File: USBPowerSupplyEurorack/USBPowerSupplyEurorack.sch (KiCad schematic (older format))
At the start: 19 parts, among them J1 1734366-1, J2 10129381-910001BLF, Q1 Q_PMOS_GSD

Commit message: connected switch to control the DC-DC converters
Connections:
- net labels added: CTRL
- net labels removed: +5VD
- no-connect marks 8 -> 6
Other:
- moved on the sheet: R1, S1
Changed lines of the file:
@@
 USB Power In
 Wire Wire Line
-	4430 1830 4430 1930
-Wire Wire Line
-	5830 1830 5830 1930
+	4690 1830 4690 1930
+Wire Wire Line
+	6090 1830 6090 1930
 $Comp
 L LP4OA1PBCTR:LP4OA1PBCTR S1
 U 1 1 5FE10AE7
-P 5130 2530
-F 0 "S1" V 6270 2840 50  0000 L CNN
-F 1 "LP4OA1PBCTR" V 6180 2640 50  0000 L CNN
-F 2 "LP4OA1PBCTR:LP4OA1PBCTR" H 6180 3030 50  0001 L CNN
-F 3 "http://spec_sheets.e-switch.com/specs/B240001.pdf" H 6180 2930 50  0001 L CNN
-F 4 "Pushbutton Switches DPDT On-Mom LED, Red" H 6180 2830 50  0001 L CNN "Description"
-F 5 "19.95" H 6180 2730 50  0001 L CNN "Height"
-F 6 "E-Switch" H 6180 2630 50  0001 L CNN "Manufacturer_Name"
-F 7 "LP4OA1PBCTR" H 6180 2530 50  0001 L CNN "Manufacturer_Part_Number"
-F 8 "" H 6180 2430 50  0001 L CNN "Arrow Part Number"
-F 9 "" H 6180 2330 50  0001 L CNN "Arrow Price/Stock"
-F 10 "612-LP4OA1PBCTR" H 6180 2230 50  0001 L CNN "Mouser Part Number"
-F 11 "https://www.mouser.com/Search/Refine.aspx?Keyword=612-LP4OA1PBCTR" H 6180 2130 50  0001 L CNN "Mouser Price/Stock"
-	1    5130 2530
+P 5390 2530
+F 0 "S1" V 6530 2840 50  0000 L CNN
+F 1 "LP4OA1PBCTR" V 6440 2640 50  0000 L CNN
+F 2 "LP4OA1PBCTR:LP4OA1PBCTR" H 6440 3030 50  0001 L CNN
+F 3 "http://spec_sheets.e-switch.com/specs/B240001.pdf" H 6440 2930 50  0001 L CNN
+F 4 "Pushbutton Switches DPDT On-Mom LED, Red" H 6440 2830 50  0001 L CNN "Description"
+F 5 "19.95" H 6440 2730 50  0001 L CNN "Height"
+F 6 "E-Switch" H 6440 2630 50  0001 L CNN "Manufacturer_Name"
+F 7 "LP4OA1PBCTR" H 6440 2530 50  0001 L CNN "Manufacturer_Part_Number"
+F 8 "" H 6440 2430 50  0001 L CNN "Arrow Part Number"
+F 9 "" H 6440 2330 50  0001 L CNN "Arrow Price/Stock"
+F 10 "612-LP4OA1PBCTR" H 6440 2230 50  0001 L CNN "Mouser Part Number"
+F 11 "https://www.mouser.com/Search/Refine.aspx?Keyword=612-LP4OA1PBCTR" H 6440 2130 50  0001 L CNN "Mouser Price/Stock"
+	1    5390 2530
 	0    -1   -1   0
 $EndComp
-NoConn ~ 4430 2030
-NoConn ~ 5830 2030
-Connection ~ 5830 1830
-$Comp
-L power:+5VD #PWR0102
-U 1 1 5FE20BD7
-P 2560 1440
-F 0 "#PWR0102" H 2560 1290 50  0001 C CNN
-F 1 "+5VD" H 2575 1613 50  0000 C CNN
-F 2 "" H 2560 1440 50  0001 C CNN
-F 3 "" H 2560 1440 50  0001 C CNN
-	1    2560 1440
-	1    0    0    -1
-$EndComp
+NoConn ~ 4690 2030
+NoConn ~ 6090 2030
+Connection ~ 6090 1830
 $Comp
 L power:+5V #PWR0103
 U 1 1 5FE2195B
-P 5830 1830
-F 0 "#PWR0103" H 5830 1680 50  0001 C CNN
-F 1 "+5V" H 5845 2003 50  0000 C CNN
-F 2 "" H 5830 1830 50  0001 C CNN
-F 3 "" H 5830 1830 50  0001 C CNN
-	1    5830 1830
-	1    0    0    -1
-$EndComp
-$Comp
-L power:+5VD #PWR0104
-U 1 1 5FE220CC
-P 4430 1830
-F 0 "#PWR0104" H 4430 1680 50  0001 C CNN
-F 1 "+5VD" H 4445 2003 50  0000 C CNN
-F 2 "" H 4430 1830 50  0001 C CNN
-F 3 "" H 4430 1830 50  0001 C CNN
-	1    4430 1830
-	1    0    0    -1
-$EndComp
-Connection ~ 4430 1830
+P 6090 1830
+F 0 "#PWR0103" H 6090 1680 50  0001 C CNN
+F 1 "+5V" H 6105 2003 50  0000 C CNN
+F 2 "" H 6090 1830 50  0001 C CNN
+F 3 "" H 6090 1830 50  0001 C CNN
+	1    6090 1830
+	1    0    0    -1
+$EndComp
 $Comp
 L Device:R_Small R1
 U 1 1 5FE234A2
-P 5130 2630
-F 0 "R1" H 5189 2676 50  0000 L CNN
-F 1 "510" H 5189 2585 50  0000 L CNN
-F 2 "Resistor_SMD:R_0612_1632Metric" H 5130 2630 50  0001 C CNN
-F 3 "~" H 5130 2630 50  0001 C CNN
-	1    5130 2630
-	1    0    0    -1
-$EndComp
-Wire Notes Line
-	4240 1010 6360 1010
+P 5390 2630
+F 0 "R1" H 5449 2676 50  0000 L CNN
+F 1 "510" H 5449 2585 50  0000 L CNN
+F 2 "Resistor_SMD:R_0612_1632Metric" H 5390 2630 50  0001 C CNN
+F 3 "~" H 5390 2630 50  0001 C CNN
+	1    5390 2630
+	1    0    0    -1
+$EndComp
 Wire Notes Line
 	6360 1010 6360 3050
-Wire Notes Line
-	6360 3050 4240 3050
-Wire Notes Line
-	4240 3050 4240 1010
 Text Notes 4240 1010 0    50   ~ 0
 Push button & LED
@@
 $EndComp
 Connection ~ 5990 5650
-$Comp
-L power:PWR_FLAG #FLG0104
-U 1 1 5FEBEC19
-P 5830 1830
-F 0 "#FLG0104" H 5830 1905 50  0001 C CNN
-F 1 "PWR_FLAG" V 5830 1958 50  0000 L CNN
-F 2 "" H 5830 1830 50  0001 C CNN
-F 3 "~" H 5830 1830 50  0001 C CNN
-	1    5830 1830
-	0    1    1    0
-$EndComp
 Wire Wire Line
 	8900 5530 9800 5530
@@
 	0    1    1    0
 $EndComp
-$Comp
-L RS6-0512S:RS6-0512S PS1
-U 1 1 5FE5CD2D
-P 1630 4780
-F 0 "PS1" H 1990 5020 50  0000 L CNN
-F 1 "RS6-0512S" H 1920 4940 50  0000 L CNN
-F 2 "RS6-0512S:RS60512S" H 2480 4880 50  0001 L CNN
-F 3 "https://componentsearchengine.com/Datasheets/1/RS6-0512S.pdf" H 2480 4780 50  0001 L CNN
-F 4 "Isolated DC/DC Converters 6W 4.5-9Vin 12Vout 500mA SIP8" H 2480 4680 50  0001 L CNN "Description"
-F 5 "11.6" H 2480 4580 50  0001 L CNN "Height"
-F 6 "RECOM Power" H 2480 4480 50  0001 L CNN "Manufacturer_Name"
-F 7 "RS6-0512S" H 2480 4380 50  0001 L CNN "Manufacturer_Part_Number"
-F 8 "919-RS6-0512S" H 2480 4280 50  0001 L CNN "Mouser Part Number"
-F 9 "https://www.mouser.co.uk/ProductDetail/RECOM-Power/RS6-0512S?qs=FLBwGrBR9%252B1rp7zTwCRMhw%3D%3D" H 2480 4180 50  0001 L CNN "Mouser Price/Stock"
-F 10 "" H 2480 4080 50  0001 L CNN "Arrow Part Number"
-F 11 "" H 2480 3980 50  0001 L CNN "Arrow Price/Stock"
-	1    1630 4780
-	1    0    0    -1
-$EndComp
 Text GLabel 1630 4780 0    50   Input ~ 0
 -Vin
 Text GLabel 1630 4880 0    50   Input ~ 0
 +Vin
-NoConn ~ 1630 4980
 Text GLabel 1560 5280 0    50   Input ~ 0
 0V
@@
 Text GLabel 1630 5920 0    50   Input ~ 0
 +Vin
-NoConn ~ 1630 6020
 Text GLabel 1560 6220 0    50   Input ~ 0
 0V
@@
 	1    0    0    -1
 $EndComp
-Text GLabel 5080 2880 0    50   Input ~ 0
+Text GLabel 5340 2880 0    50   Input ~ 0
 0V
 Wire Wire Line
-	5080 2880 5130 2880
-Wire Wire Line
-	5130 2730 5130 2880
-Text GLabel 5080 1230 0    50   Input ~ 0
+	5340 2880 5390 2880
+Wire Wire Line
+	5390 2730 5390 2880
+Text GLabel 5340 1230 0    50   Input ~ 0
 +12V
 Wire Wire Line
-	5080 1230 5130 1230
-Wire Wire Line
-	5130 1230 5130 1330
+	5340 1230 5390 1230
+Wire Wire Line
+	5390 1230 5390 1330
 $Comp
 L eec2:ACM4520V-901-2P-T L1
@@
 Wire Wire Line
 	8440 2380 8800 2380
+$Comp
+L power:+5V #PWR?
+U 1 1 5FE7630F
+P 2560 1440
+F 0 "#PWR?" H 2560 1290 50  0001 C CNN
+F 1 "+5V" H 2575 1613 50  0000 C CNN
+F 2 "" H 2560 1440 50  0001 C CNN
+F 3 "" H 2560 1440 50  0001 C CNN
+	1    2560 1440
+	1    0    0    -1
+$EndComp
+Text GLabel 1630 4980 0    50   Input ~ 0
+CTRL
+$Comp
+L RS6-0512S:RS6-0512S PS1
+U 1 1 5FE5CD2D
+P 1630 4780
+F 0 "PS1" H 1990 5020 50  0000 L CNN
+F 1 "RS6-0512S" H 1920 4940 50  0000 L CNN
+F 2 "RS6-0512S:RS60512S" H 2480 4880 50  0001 L CNN
+F 3 "https://componentsearchengine.com/Datasheets/1/RS6-0512S.pdf" H 2480 4780 50  0001 L CNN
+F 4 "Isolated DC/DC Converters 6W 4.5-9Vin 12Vout 500mA SIP8" H 2480 4680 50  0001 L CNN "Description"
+F 5 "11.6" H 2480 4580 50  0001 L CNN "Height"
+F 6 "RECOM Power" H 2480 4480 50  0001 L CNN "Manufacturer_Name"
+F 7 "RS6-0512S" H 2480 4380 50  0001 L CNN "Manufacturer_Part_Number"
+F 8 "919-RS6-0512S" H 2480 4280 50  0001 L CNN "Mouser Part Number"
+F 9 "https://www.mouser.co.uk/ProductDetail/RECOM-Power/RS6-0512S?qs=FLBwGrBR9%252B1rp7zTwCRMhw%3D%3D" H 2480 4180 50  0001 L CNN "Mouser Price/Stock"
+F 10 "" H 2480 4080 50  0001 L CNN "Arrow Part Number"
+F 11 "" H 2480 3980 50  0001 L CNN "Arrow Price/Stock"
+	1    1630 4780
+	1    0    0    -1
+$EndComp
+Text GLabel 1630 6020 0    50   Input ~ 0
+CTRL
+Wire Notes Line
+	6360 3050 4240 3050
+Wire Notes Line
+	4240 3050 4240 1010
+Wire Notes Line
+	4240 1010 6360 1010
+Text GLabel 4690 1830 0    50   Input ~ 0
+CTRL
 $EndSCHEMATC

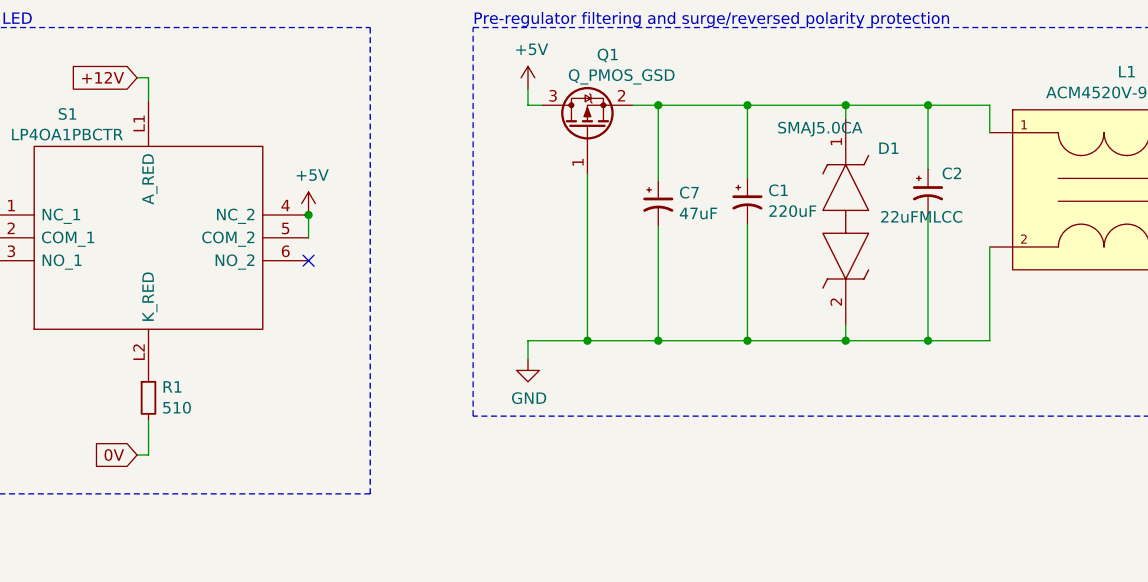
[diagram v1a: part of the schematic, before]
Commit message: changing footprints for JLC available parts
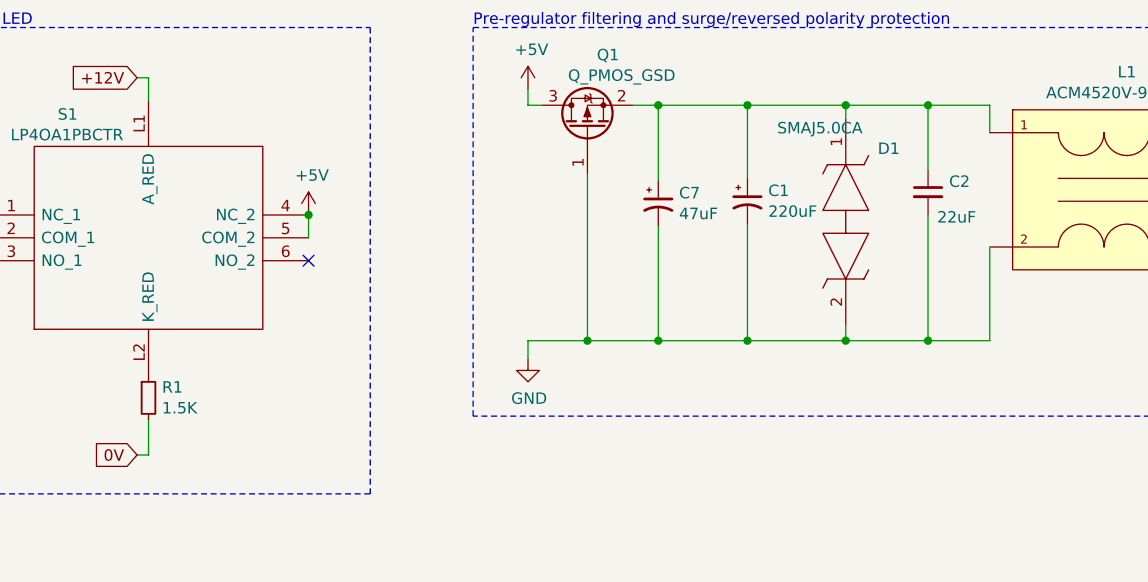
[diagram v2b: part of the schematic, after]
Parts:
- removed C2: 22uFMLCC, Capacitor_SMD:C_1210_3225Metric, symbol Device:CP1_Small
- added C2: 22uF, Capacitor_SMD:C_0805_2012Metric, symbol Device:C_Small
- C1: footprint Capacitor_SMD:C_Elec_8x10.2 -> Capacitor_SMD:C_Elec_6.3x7.7; LCSC (none) -> C127327
- C7: footprint Capacitor_SMD:C_Elec_6.3x5.8 -> Capacitor_SMD:C_Elec_5x5.4; LCSC (none) -> C294514
- D1: footprint DIONM5026X229N -> digikey-footprints:DO-214AC; LCSC (none) -> C151931
- F1: footprint 1812L110_16DR:FUSC4632X125N -> Fuse:Fuse_1812_4532Metric; LCSC (none) -> C163516
- L1: LCSC (none) -> C92126
- Q1: LCSC (none) -> C15127
- R1: value 510 -> 1.5K; footprint Resistor_SMD:R_0612_1632Metric -> Resistor_SMD:R_0805_2012Metric; LCSC (none) -> C4310
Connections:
- net GND: now also C2.2
- net at C1.1, C7.1, D1.1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: now also C2.1
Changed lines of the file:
@@
 F 0 "C1" H 8101 1816 50  0000 L CNN
 F 1 "220uF" H 8101 1725 50  0000 L CNN
-F 2 "Capacitor_SMD:C_Elec_8x10.2" H 8010 1770 50  0001 C CNN
+F 2 "Capacitor_SMD:C_Elec_6.3x7.7" H 8010 1770 50  0001 C CNN
 F 3 "~" H 8010 1770 50  0001 C CNN
+F 4 "C127327" H 8010 1770 50  0001 C CNN "LCSC"
 	1    8010 1770
 	1    0    0    -1
@@
 P 5390 2630
 F 0 "R1" H 5449 2676 50  0000 L CNN
-F 1 "510" H 5449 2585 50  0000 L CNN
-F 2 "Resistor_SMD:R_0612_1632Metric" H 5390 2630 50  0001 C CNN
+F 1 "1.5K" H 5449 2585 50  0000 L CNN
+F 2 "Resistor_SMD:R_0805_2012Metric" H 5390 2630 50  0001 C CNN
 F 3 "~" H 5390 2630 50  0001 C CNN
+F 4 "C4310" H 5390 2630 50  0001 C CNN "LCSC"
 	1    5390 2630
 	1    0    0    -1
@@
 NoConn ~ 1660 1590
 NoConn ~ 1660 1690
-$Comp
-L Device:CP1_Small C2
-U 1 1 5FE2664F
-P 8800 1730
-F 0 "C2" H 8860 1810 50  0000 L CNN
-F 1 "22uFMLCC" H 8590 1620 50  0000 L CNN
-F 2 "Capacitor_SMD:C_1210_3225Metric" H 8800 1730 50  0001 C CNN
-F 3 "~" H 8800 1730 50  0001 C CNN
-	1    8800 1730
-	1    0    0    -1
-$EndComp
 Wire Wire Line
 	8010 1670 8010 1350
@@
 F 0 "C7" H 7711 1826 50  0000 L CNN
 F 1 "47uF" H 7711 1735 50  0000 L CNN
-F 2 "Capacitor_SMD:C_Elec_6.3x5.8" H 7620 1780 50  0001 C CNN
+F 2 "Capacitor_SMD:C_Elec_5x5.4" H 7620 1780 50  0001 C CNN
 F 3 "~" H 7620 1780 50  0001 C CNN
+F 4 "C294514" H 7620 1780 50  0001 C CNN "LCSC"
 	1    7620 1780
 	1    0    0    -1
@@
 F 0 "F1" H 2130 1715 50  0000 C CNN
 F 1 "1812L110" H 2130 1624 50  0000 C CNN
-F 2 "1812L110_16DR:FUSC4632X125N" H 2330 1540 50  0001 L CNN
+F 2 "Fuse:Fuse_1812_4532Metric" H 2330 1540 50  0001 L CNN
 F 3 "https://www.arrow.com/en/products/1812l11016dr/littelfuse" H 2330 1440 50  0001 L CNN
 F 4 "PTC Resettable Fuse 1.1A(hold) 1.95A(trip) 8VDC 100A 0.8W 0.3s 0.06Ohm SMD Solder Pad 1812 T/R" H 2330 1340 50  0001 L CNN "Description"
@@
 F 10 "576-1812L110/16DR" H 2330 740 50  0001 L CNN "Mouser Part Number"
 F 11 "https://www.mouser.co.uk/ProductDetail/Littelfuse/1812L110-16DR?qs=PWhpLWeW8we3Ga3SZHmLHg%3D%3D" H 2330 640 50  0001 L CNN "Mouser Price/Stock"
+F 12 "C163516" H 1780 1490 50  0001 C CNN "LCSC"
 	1    1780 1490
 	1    0    0    -1
@@
 F 2 "digikey-footprints:SOT-23-3" H 7510 1550 50  0001 C CNN
 F 3 "https://www.mouser.fr/datasheet/2/916/PMV240SP-1919536.pdf" H 7310 1450 50  0001 C CNN
+F 4 "C15127" V 7310 1450 50  0001 C CNN "LCSC"
 	1    7310 1450
 	0    -1   -1   0
@@
 F 14 "-40°C" H 8970 3070 50  0001 L CNN "temperature range low"
 F 15 "50V" H 8970 3170 50  0001 L CNN "voltage"
+F 16 "C92126" H 8970 1470 50  0001 C CNN "LCSC"
 	1    8970 1470
 	1    0    0    -1
@@
 F 0 "D1" V 8570 1550 50  0000 L CNN
 F 1 "SMAJ5.0CA" V 8480 1110 50  0000 L CNN
-F 2 "DIONM5026X229N" H 9040 1560 50  0001 L BNN
+F 2 "digikey-footprints:DO-214AC" H 9040 1560 50  0001 L BNN
 F 3 "http://www.littelfuse.com/~/media/electronics/datasheets/tvs_diodes/littelfuse_tvs_diode_smaj_datasheet.pdf.pdf" H 9040 1460 50  0001 L BNN
 F 4 "Littelfuse SMAJ5.0CA Bi-Directional TVS Diode, 400W peak, 2-Pin DO-214AC" H 9040 1360 50  0001 L BNN "Description"
@@
 F 10 "SMAJ5.0CA" H 9040 760 50  0001 L BNN "Arrow Part Number"
 F 11 "https://www.arrow.com/en/products/smaj5.0ca/littelfuse" H 9040 660 50  0001 L BNN "Arrow Price/Stock"
+F 12 "C151931" H 8440 1410 50  0001 C CNN "LCSC"
 	1    8440 1410
 	0    1    1    0
@@
 F 10 "" H 2480 4080 50  0001 L CNN "Arrow Part Number"
 F 11 "" H 2480 3980 50  0001 L CNN "Arrow Price/Stock"
+F 12 "" H 1630 4780 50  0001 C CNN "LCSC"
 	1    1630 4780
 	1    0    0    -1
@@
 Text GLabel 4690 1830 0    50   Input ~ 0
 CTRL
+$Comp
+L Device:C_Small C2
+U 1 1 5FEA4264
+P 8800 1730
+F 0 "C2" H 8892 1776 50  0000 L CNN
+F 1 "22uF" H 8840 1620 50  0000 L CNN
+F 2 "Capacitor_SMD:C_0805_2012Metric" H 8800 1730 50  0001 C CNN
+F 3 "~" H 8800 1730 50  0001 C CNN
+F 4 " C45783" H 8800 1730 50  0001 C CNN "LCSC"
+	1    8800 1730
+	1    0    0    -1
+$EndComp
 $EndSCHEMATC
